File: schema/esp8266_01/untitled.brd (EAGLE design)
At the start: 44.1 x 58.4 mm, 26 parts, among them IC1 LD117AS33TR, J1 DCJ0202, Q1 BC857ASMD, X2 12 MHz

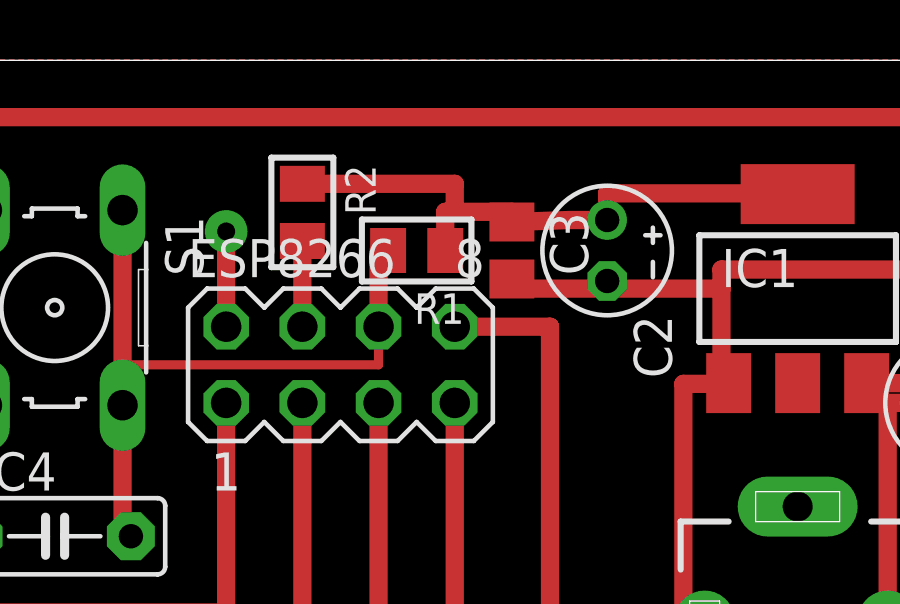
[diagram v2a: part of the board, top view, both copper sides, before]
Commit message: Added second variant of esp8266
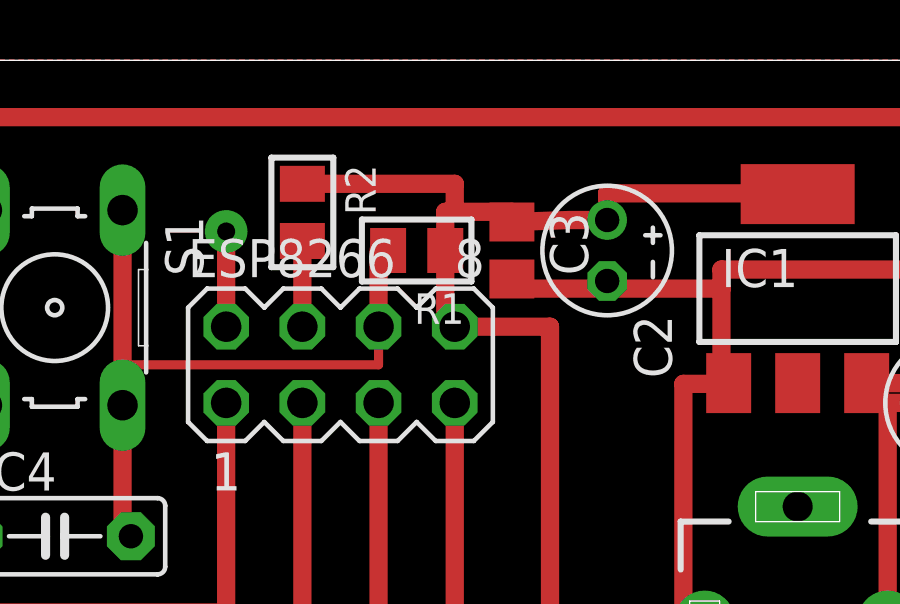
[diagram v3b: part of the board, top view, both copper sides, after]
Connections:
- net GND: now also U$1.1
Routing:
- net VCC: track 77.0 -> 79.8 mm
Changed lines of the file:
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@@
 <layer number="101" name="Gehäuse" color="7" fill="1" visible="no" active="yes"/>
 <layer number="102" name="Mittellin" color="7" fill="1" visible="no" active="yes"/>
-<layer number="103" name="tMap" color="7" fill="1" visible="yes" active="yes"/>
+<layer number="103" name="tMap" color="7" fill="1" visible="no" active="yes"/>
 <layer number="104" name="Name" color="7" fill="1" visible="no" active="yes"/>
-<layer number="105" name="tPlate" color="7" fill="1" visible="yes" active="yes"/>
-<layer number="106" name="bPlate" color="7" fill="1" visible="yes" active="yes"/>
-<layer number="107" name="Crop" color="7" fill="1" visible="yes" active="yes"/>
+<layer number="105" name="tPlate" color="7" fill="1" visible="no" active="yes"/>
+<layer number="106" name="bPlate" color="7" fill="1" visible="no" active="yes"/>
+<layer number="107" name="Crop" color="7" fill="1" visible="no" active="yes"/>
 <layer number="108" name="fp8" color="7" fill="1" visible="no" active="yes"/>
 <layer number="109" name="fp9" color="7" fill="1" visible="no" active="yes"/>
 <layer number="110" name="fp0" color="7" fill="1" visible="no" active="yes"/>
-<layer number="116" name="Patch_BOT" color="9" fill="4" visible="yes" active="yes"/>
-<layer number="121" name="_tsilk" color="7" fill="1" visible="yes" active="yes"/>
-<layer number="122" name="_bsilk" color="7" fill="1" visible="yes" active="yes"/>
+<layer number="116" name="Patch_BOT" color="9" fill="4" visible="no" active="yes"/>
+<layer number="121" name="_tsilk" color="7" fill="1" visible="no" active="yes"/>
+<layer number="122" name="_bsilk" color="7" fill="1" visible="no" active="yes"/>
 <layer number="123" name="tTestmark" color="7" fill="1" visible="no" active="yes"/>
 <layer number="124" name="bTestmark" color="7" fill="1" visible="no" active="yes"/>
@@
 <layer number="131" name="tAdjust" color="7" fill="1" visible="no" active="yes"/>
 <layer number="132" name="bAdjust" color="7" fill="1" visible="no" active="yes"/>
-<layer number="144" name="Drill_legend" color="7" fill="1" visible="yes" active="yes"/>
+<layer number="144" name="Drill_legend" color="7" fill="1" visible="no" active="yes"/>
 <layer number="151" name="HeatSink" color="7" fill="1" visible="no" active="yes"/>
-<layer number="199" name="Contour" color="7" fill="1" visible="yes" active="yes"/>
+<layer number="199" name="Contour" color="7" fill="1" visible="no" active="yes"/>
 <layer number="200" name="200bmp" color="1" fill="10" visible="no" active="no"/>
-<layer number="201" name="201bmp" color="2" fill="10" visible="yes" active="yes"/>
-<layer number="202" name="202bmp" color="3" fill="10" visible="yes" active="yes"/>
-<layer number="203" name="203bmp" color="4" fill="10" visible="yes" active="yes"/>
-<layer number="204" name="204bmp" color="5" fill="10" visible="yes" active="yes"/>
-<layer number="205" name="205bmp" color="6" fill="10" visible="yes" active="yes"/>
-<layer number="206" name="206bmp" color="7" fill="10" visible="yes" active="yes"/>
-<layer number="207" name="207bmp" color="8" fill="10" visible="yes" active="yes"/>
-<layer number="208" name="208bmp" color="9" fill="10" visible="yes" active="yes"/>
-<layer number="209" name="209bmp" color="7" fill="1" visible="yes" active="yes"/>
-<layer number="210" name="210bmp" color="7" fill="1" visible="yes" active="yes"/>
-<layer number="211" name="211bmp" color="7" fill="1" visible="yes" active="yes"/>
-<layer number="212" name="212bmp" color="7" fill="1" visible="yes" active="yes"/>
-<layer number="213" name="213bmp" color="7" fill="1" visible="yes" active="yes"/>
-<layer number="214" name="214bmp" color="7" fill="1" visible="yes" active="yes"/>
-<layer number="215" name="215bmp" color="7" fill="1" visible="yes" active="yes"/>
-<layer number="216" name="216bmp" color="7" fill="1" visible="yes" active="yes"/>
+<layer number="201" name="201bmp" color="2" fill="10" visible="no" active="yes"/>
+<layer number="202" name="202bmp" color="3" fill="10" visible="no" active="yes"/>
+<layer number="203" name="203bmp" color="4" fill="10" visible="no" active="yes"/>
+<layer number="204" name="204bmp" color="5" fill="10" visible="no" active="yes"/>
+<layer number="205" name="205bmp" color="6" fill="10" visible="no" active="yes"/>
+<layer number="206" name="206bmp" color="7" fill="10" visible="no" active="yes"/>
+<layer number="207" name="207bmp" color="8" fill="10" visible="no" active="yes"/>
+<layer number="208" name="208bmp" color="9" fill="10" visible="no" active="yes"/>
+<layer number="209" name="209bmp" color="7" fill="1" visible="no" active="yes"/>
+<layer number="210" name="210bmp" color="7" fill="1" visible="no" active="yes"/>
+<layer number="211" name="211bmp" color="7" fill="1" visible="no" active="yes"/>
+<layer number="212" name="212bmp" color="7" fill="1" visible="no" active="yes"/>
+<layer number="213" name="213bmp" color="7" fill="1" visible="no" active="yes"/>
+<layer number="214" name="214bmp" color="7" fill="1" visible="no" active="yes"/>
+<layer number="215" name="215bmp" color="7" fill="1" visible="no" active="yes"/>
+<layer number="216" name="216bmp" color="7" fill="1" visible="no" active="yes"/>
 <layer number="217" name="217bmp" color="18" fill="1" visible="no" active="no"/>
 <layer number="218" name="218bmp" color="19" fill="1" visible="no" active="no"/>
@@
 <wire x1="47.625" y1="26.67" x2="47.655" y2="26.67" width="0.3048" layer="1"/>
 <wire x1="47.655" y1="26.67" x2="47.655" y2="28.655" width="0.3048" layer="1"/>
+<contactref element="U$1" pad="1"/>
+<wire x1="21.59" y1="49.53" x2="29.055" y2="48.26" width="0" layer="19" extent="1-1"/>
 </signal>
 <signal name="VCC">
@@
 <wire x1="34.445" y1="48.26" x2="37.465" y2="48.26" width="0.6096" layer="1"/>
 <wire x1="37.465" y1="48.26" x2="37.465" y2="57.15" width="0.6096" layer="1"/>
-<wire x1="34.29" y1="73.66" x2="33.9725" y2="76.2" width="0" layer="19" extent="1-1"/>
+<wire x1="34.29" y1="73.66" x2="33.9725" y2="73.66" width="0.6096" layer="1"/>
+<wire x1="33.9725" y1="73.66" x2="33.9725" y2="76.2" width="0.6096" layer="1"/>
 </signal>
 <signal name="RESET">

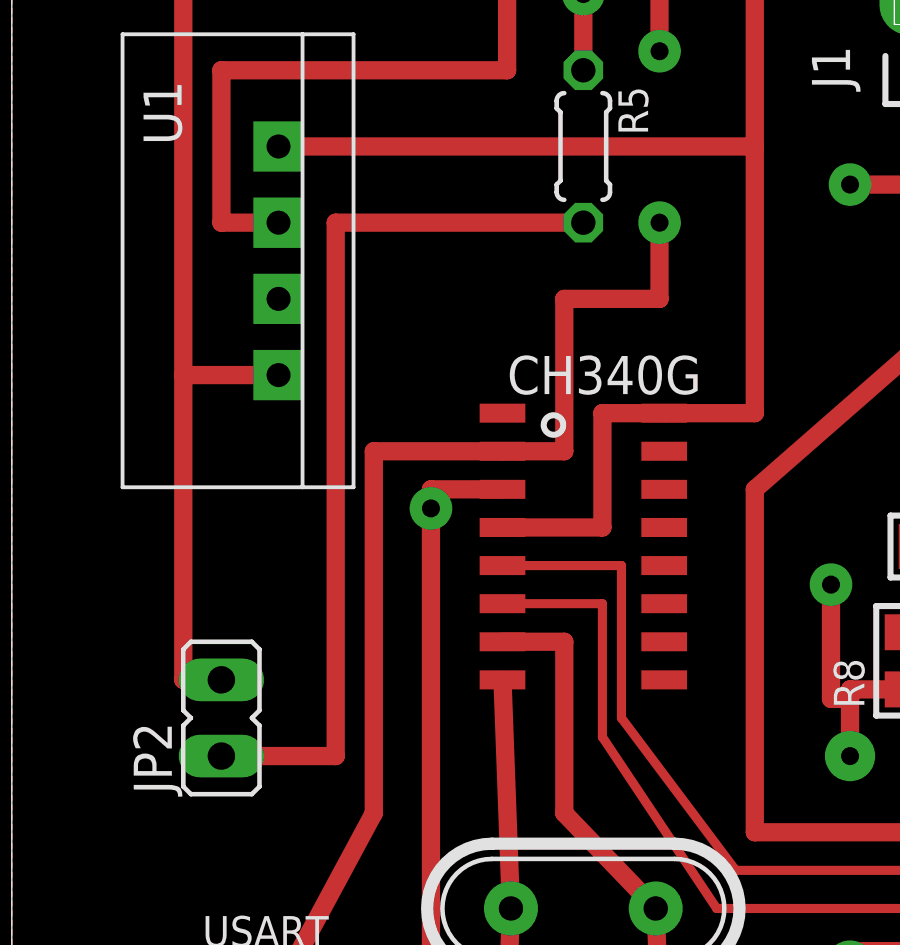
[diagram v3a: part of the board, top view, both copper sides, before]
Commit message: fixed power for usb-usart
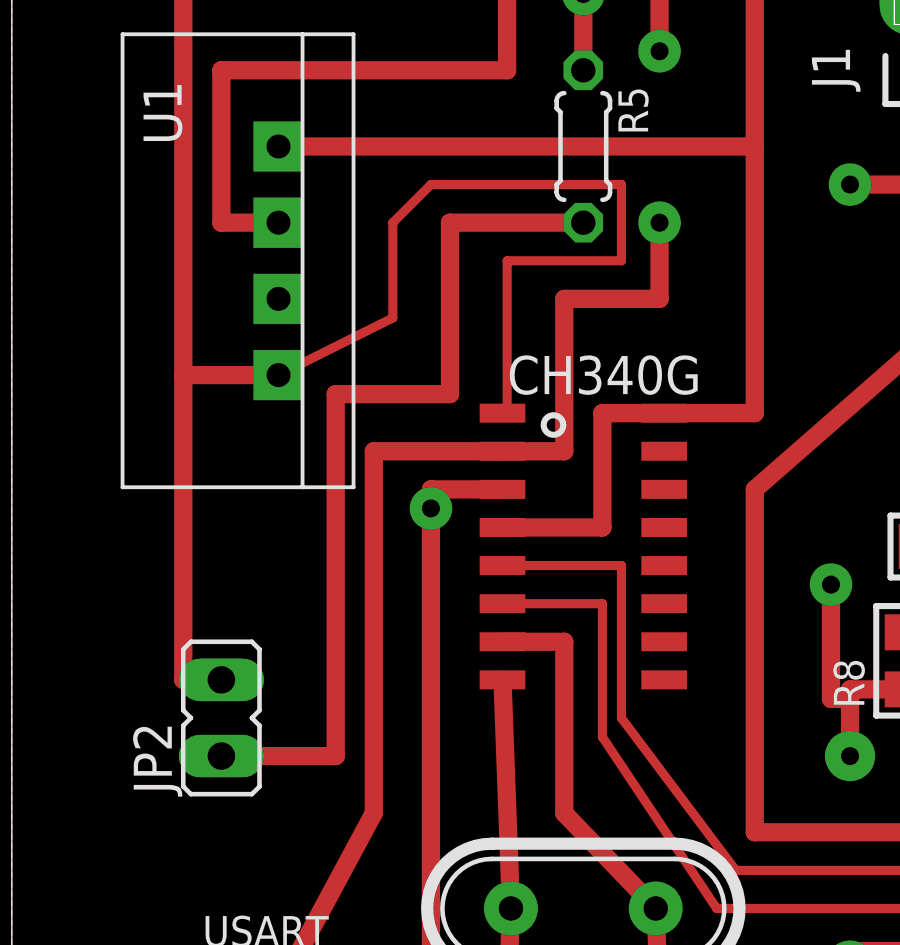
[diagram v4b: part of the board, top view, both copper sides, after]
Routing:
- net GND: track 232.6 -> 259.8 mm
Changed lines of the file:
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@@
 <wire x1="47.655" y1="26.67" x2="47.655" y2="28.655" width="0.3048" layer="1"/>
 <contactref element="U$1" pad="1"/>
-<wire x1="21.59" y1="49.53" x2="29.055" y2="48.26" width="0" layer="19" extent="1-1"/>
+<wire x1="29.055" y1="48.26" x2="29.21" y2="48.26" width="0.3048" layer="1"/>
+<wire x1="29.21" y1="48.26" x2="29.21" y2="53.34" width="0.3048" layer="1"/>
+<wire x1="29.21" y1="53.34" x2="33.02" y2="53.34" width="0.3048" layer="1"/>
+<wire x1="33.02" y1="53.34" x2="33.02" y2="55.88" width="0.3048" layer="1"/>
+<wire x1="33.02" y1="55.88" x2="26.67" y2="55.88" width="0.3048" layer="1"/>
+<wire x1="26.67" y1="55.88" x2="25.4" y2="54.61" width="0.3048" layer="1"/>
+<wire x1="25.4" y1="54.61" x2="25.4" y2="51.435" width="0.3048" layer="1"/>
+<wire x1="25.4" y1="51.435" x2="21.59" y2="49.53" width="0.3048" layer="1"/>
 </signal>
 <signal name="VCC">
@@
 <contactref element="R5" pad="2"/>
 <contactref element="JP2" pad="1"/>
-<wire x1="31.75" y1="54.61" x2="23.495" y2="54.61" width="0.6096" layer="1"/>
-<wire x1="23.495" y1="54.61" x2="23.495" y2="36.83" width="0.6096" layer="1"/>
+<wire x1="31.75" y1="54.61" x2="27.305" y2="54.61" width="0.6096" layer="1"/>
+<wire x1="27.305" y1="54.61" x2="27.305" y2="48.895" width="0.6096" layer="1"/>
+<wire x1="27.305" y1="48.895" x2="23.495" y2="48.895" width="0.6096" layer="1"/>
+<wire x1="23.495" y1="48.895" x2="23.495" y2="36.83" width="0.6096" layer="1"/>
 <wire x1="23.495" y1="36.83" x2="19.685" y2="36.83" width="0.6096" layer="1"/>
 </signal>

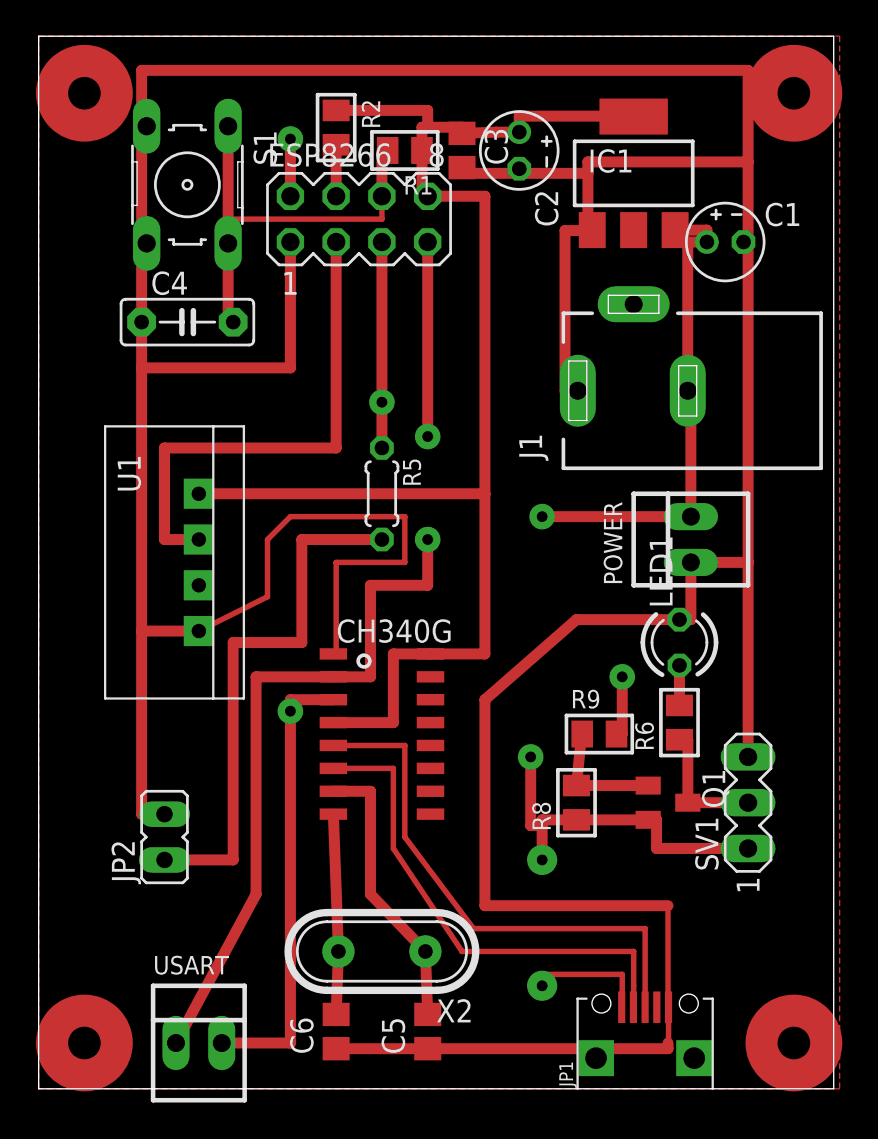
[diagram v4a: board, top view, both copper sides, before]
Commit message: Minimised schema var 1
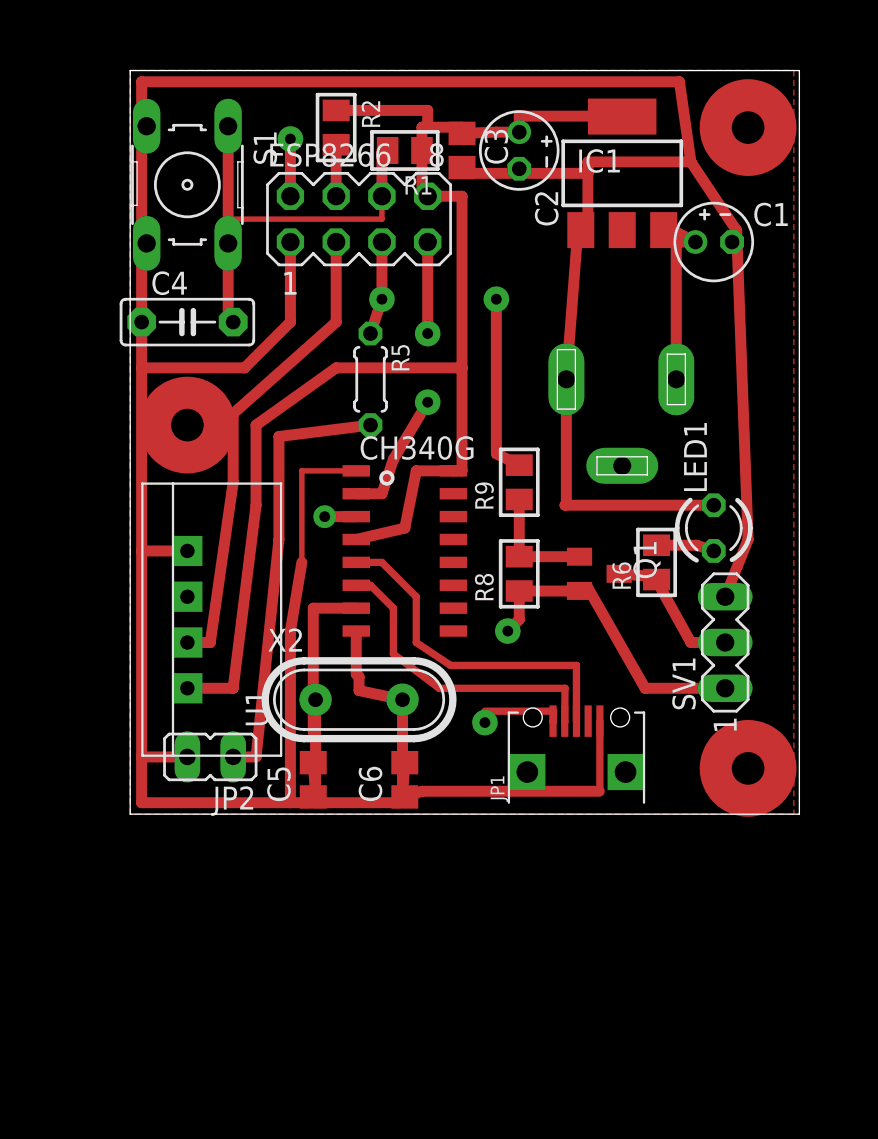
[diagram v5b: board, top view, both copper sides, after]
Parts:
- removed POWER, USART: 22-23-2021, con-molex:22-23-2021
- moved JP1 16.3 mm to (42.5, 40.0)
- moved C5 15.3 mm to (27.9, 41.3)
- moved R9 14.7 mm to (39.4, 57.8), turned to 90 degrees
- moved C6 14.5 mm to (33.0, 41.3)
- moved X2 14.0 mm to (30.5, 45.7), turned to 0 degrees
- moved Q1 13.3 mm to (43.8, 52.7)
- moved R8 13.1 mm to (39.4, 52.7)
- moved U$1 10.2 mm to (33.0, 54.0)
- moved SV1 8.98 mm to (50.8, 48.9)
- moved R6 8.98 mm to (47.0, 53.3)
- moved LED1 6.63 mm to (50.2, 55.2)
- moved R5 6.38 mm to (31.1, 63.5)
- moved JP2 5.12 mm to (22.2, 42.5), turned to 90 degrees
- moved U1 3.24 mm to (21.0, 50.2), turned to 90 degrees
- moved J1 0.90 mm to (45.1, 63.5), flipped to the bottom, turned to 270 degrees
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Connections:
- new net S$1: C1.+, IC1.3, J1.3
- net GND: no longer POWER.1
- net N$37: no longer C1.+, IC1.3, J1.3, POWER.2
- net RX: no longer USART.2
- net TX: no longer USART.1
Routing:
- net GND: track 259.8 -> 211.9 mm
- net TX: track 49.4 -> 12.2 mm
- net N$37: track 53.8 -> 19.2 mm, vias 4 -> 0
- net RX: track 28.4 -> 4.92 mm, vias 2 -> 1
- net S$1: track 0.00 -> 10.6 mm
- net N$31: track 29.3 -> 19.0 mm
- net N$29: track 27.3 -> 17.2 mm
- net N$1: track 29.8 -> 24.2 mm
- net N$27: track 15.7 -> 18.1 mm
- net S$2: track 0.00 -> 2.17 mm, vias 0 -> 2
- net GPIO2: track 27.9 -> 26.2 mm
- net N$28: track 11.1 -> 12.9 mm
- net N$32: track 2.22 -> 3.23 mm
- net N$3: track 7.49 -> 6.52 mm
- net N$7: track 7.30 -> 8.03 mm
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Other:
- board size 44.1 x 58.4 mm -> 37.1 x 41.3 mm
